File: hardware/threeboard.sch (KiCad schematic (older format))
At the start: 49 parts, among them J1 USB_mini_micro_B, K1 KEYSW, K2 KEYSW, K3 KEYSW, SW1 SW_PUSH, U1 ATMEGA32U4, U2 24LC512, X1 XTAL_GND

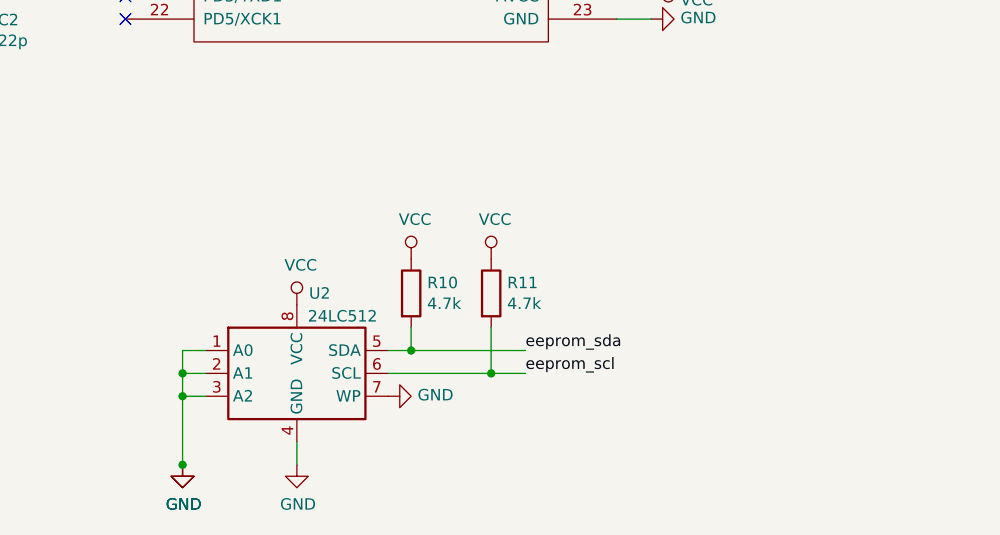
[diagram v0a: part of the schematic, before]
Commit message: Add v1 hardware revision with reinforced USB, better LED placement, and dual SMD EEPROM
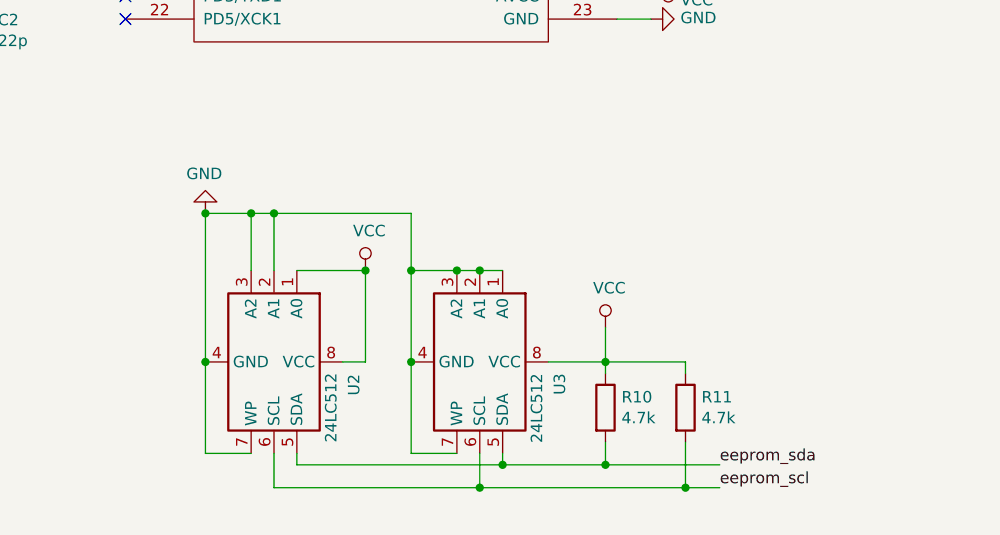
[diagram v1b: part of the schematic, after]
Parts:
- added U3: 24LC512, 24LC512-I_MF:DFN500X600X95-9N, symbol Memory_EEPROM:24LC512
- J1: footprint 10118194-0001LF:AMPHENOL_10118194-0001LF -> USB3070-XX-X_REVE:GCT_USB3070-XX-X_REVE
- SW1: footprint Button_Switch_SMD:SW_SPST_TL3342 -> PTS526_SK08_SMTR2_LFS:SW_PTS526_SK08_SMTR2_LFS
- U2: footprint 24LC512:SOIC127P794X203-8N -> 24LC512-I_MF:DFN500X600X95-9N
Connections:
- net GND: now also U3.1 (A0), U3.2 (A1), U3.3 (A2), U3.4 (GND), U3.7 (WP); no longer U2.1 (A0)
- net VCC: now also U2.1 (A0), U3.8 (VCC)
- net eeprom_scl: now also U3.6 (SCL)
- net eeprom_sda: now also U3.5 (SDA)
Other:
- moved on the sheet: R10, R11, U2
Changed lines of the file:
@@
 EESchema Schematic File Version 4
-LIBS:threeboard-cache
 EELAYER 30 0
 EELAYER END
@@
 F 0 "SW1" H 2000 4200 50  0000 C CNN
 F 1 "SW_PUSH" H 2000 4150 50  0001 C CNN
-F 2 "Button_Switch_SMD:SW_SPST_TL3342" H 2000 4250 60  0001 C CNN
+F 2 "PTS526_SK08_SMTR2_LFS:SW_PTS526_SK08_SMTR2_LFS" H 2000 4250 60  0001 C CNN
 F 3 "" H 2000 4250 60  0000 C CNN
 	1    2000 4250
@@
 F 0 "J1" H 1687 3591 60  0000 C CNN
 F 1 "USB_mini_micro_B" H 1650 3550 60  0001 C CNN
-F 2 "10118194-0001LF:AMPHENOL_10118194-0001LF" H 1750 3300 60  0001 C CNN
+F 2 "USB3070-XX-X_REVE:GCT_USB3070-XX-X_REVE" H 1750 3300 60  0001 C CNN
 F 3 "" H 1750 3300 60  0000 C CNN
 	1    1800 3300
@@
 NoConn ~ 4900 4250
 $Comp
-L power:GND #PWR0117
-U 1 1 5DEAE5F0
-P 3000 7100
-F 0 "#PWR0117" H 3000 6850 50  0001 C CNN
-F 1 "GND" H 3005 6927 50  0000 C CNN
-F 2 "" H 3000 7100 50  0001 C CNN
-F 3 "" H 3000 7100 50  0001 C CNN
-	1    3000 7100
-	1    0    0    -1
-$EndComp
-Wire Wire Line
-	3100 6600 3000 6600
-Wire Wire Line
-	3000 6600 3000 6700
-Wire Wire Line
-	3100 6700 3000 6700
-Connection ~ 3000 6700
-Wire Wire Line
-	3000 6700 3000 6800
-Wire Wire Line
-	3000 6800 3100 6800
-Connection ~ 3000 6800
-Wire Wire Line
-	3000 6800 3000 7100
-$Comp
-L power:GND #PWR0120
-U 1 1 5DEC54E2
-P 3000 7100
-F 0 "#PWR0120" H 3000 6850 50  0001 C CNN
-F 1 "GND" H 3005 6927 50  0000 C CNN
-F 2 "" H 3000 7100 50  0001 C CNN
-F 3 "" H 3000 7100 50  0001 C CNN
-	1    3000 7100
-	1    0    0    -1
-$EndComp
-Connection ~ 3000 7100
-$Comp
 L power:GND #PWR0121
 U 1 1 5DEC62E8
-P 3500 7100
-F 0 "#PWR0121" H 3500 6850 50  0001 C CNN
-F 1 "GND" H 3505 6927 50  0000 C CNN
-F 2 "" H 3500 7100 50  0001 C CNN
-F 3 "" H 3500 7100 50  0001 C CNN
-	1    3500 7100
-	1    0    0    -1
-$EndComp
-Wire Wire Line
-	3500 7000 3500 7100
-$Comp
-L power:GND #PWR0122
-U 1 1 5DED20A3
-P 3900 6800
-F 0 "#PWR0122" H 3900 6550 50  0001 C CNN
-F 1 "GND" V 3905 6672 50  0000 R CNN
-F 2 "" H 3900 6800 50  0001 C CNN
-F 3 "" H 3900 6800 50  0001 C CNN
-	1    3900 6800
-	0    -1   -1   0
-$EndComp
-$Comp
-L power:VCC #PWR0123
-U 1 1 5DED2ECF
-P 3500 6400
-F 0 "#PWR0123" H 3500 6250 50  0001 C CNN
-F 1 "VCC" H 3517 6573 50  0000 C CNN
-F 2 "" H 3500 6400 50  0001 C CNN
-F 3 "" H 3500 6400 50  0001 C CNN
-	1    3500 6400
-	1    0    0    -1
-$EndComp
-$Comp
-L Memory_EEPROM:24LC512 U2
-U 1 1 5DEACBF7
-P 3500 6700
-F 0 "U2" H 3600 7050 50  0000 C CNN
-F 1 "24LC512" H 3700 6950 50  0000 C CNN
-F 2 "24LC512:SOIC127P794X203-8N" H 3500 6700 50  0001 C CNN
-F 3 "http://ww1.microchip.com/downloads/en/DeviceDoc/21754M.pdf" H 3500 6700 50  0001 C CNN
-	1    3500 6700
-	1    0    0    -1
-$EndComp
-Text Label 4500 6700 0    50   ~ 0
+P 3100 6000
+F 0 "#PWR0121" H 3100 5750 50  0001 C CNN
+F 1 "GND" H 3105 5827 50  0000 C CNN
+F 2 "" H 3100 6000 50  0001 C CNN
+F 3 "" H 3100 6000 50  0001 C CNN
+	1    3100 6000
+	-1   0    0    1
+$EndComp
+Text Label 5350 7200 0    50   ~ 0
 eeprom_scl
 $Comp
 L Device:R R10
 U 1 1 5DEE15C4
-P 4000 6350
-F 0 "R10" H 4070 6396 50  0000 L CNN
-F 1 "4.7k" H 4070 6305 50  0000 L CNN
-F 2 "Resistor_SMD:R_0805_2012Metric_Pad1.15x1.40mm_HandSolder" V 3930 6350 50  0001 C CNN
-F 3 "~" H 4000 6350 50  0001 C CNN
-	1    4000 6350
-	1    0    0    -1
-$EndComp
-$Comp
-L power:VCC #PWR0124
-U 1 1 5DEE1CFE
-P 4000 6200
-F 0 "#PWR0124" H 4000 6050 50  0001 C CNN
-F 1 "VCC" H 4017 6373 50  0000 C CNN
-F 2 "" H 4000 6200 50  0001 C CNN
-F 3 "" H 4000 6200 50  0001 C CNN
-	1    4000 6200
-	1    0    0    -1
-$EndComp
-Wire Wire Line
-	3900 6600 4000 6600
-Wire Wire Line
-	4000 6600 4000 6500
-Text Label 4500 6600 0    50   ~ 0
+P 4850 6850
+F 0 "R10" H 4920 6896 50  0000 L CNN
+F 1 "4.7k" H 4920 6805 50  0000 L CNN
+F 2 "Resistor_SMD:R_0805_2012Metric_Pad1.15x1.40mm_HandSolder" V 4780 6850 50  0001 C CNN
+F 3 "~" H 4850 6850 50  0001 C CNN
+	1    4850 6850
+	1    0    0    -1
+$EndComp
+Wire Wire Line
+	4850 7100 4850 7000
+Text Label 5350 7100 0    50   ~ 0
 eeprom_sda
-Connection ~ 4000 6600
+Connection ~ 4850 7100
 $Comp
 L Device:C_Small C4
@@
 L Device:R R11
 U 1 1 5E419777
-P 4350 6350
-F 0 "R11" H 4420 6396 50  0000 L CNN
-F 1 "4.7k" H 4420 6305 50  0000 L CNN
-F 2 "Resistor_SMD:R_0805_2012Metric_Pad1.15x1.40mm_HandSolder" V 4280 6350 50  0001 C CNN
-F 3 "~" H 4350 6350 50  0001 C CNN
-	1    4350 6350
-	1    0    0    -1
-$EndComp
-Wire Wire Line
-	4000 6600 4500 6600
-Wire Wire Line
-	3900 6700 4350 6700
-Wire Wire Line
-	4350 6500 4350 6700
-Connection ~ 4350 6700
-Wire Wire Line
-	4350 6700 4500 6700
-$Comp
-L power:VCC #PWR0125
-U 1 1 5E430356
-P 4350 6200
-F 0 "#PWR0125" H 4350 6050 50  0001 C CNN
-F 1 "VCC" H 4367 6373 50  0000 C CNN
-F 2 "" H 4350 6200 50  0001 C CNN
-F 3 "" H 4350 6200 50  0001 C CNN
-	1    4350 6200
-	1    0    0    -1
-$EndComp
+P 5200 6850
+F 0 "R11" H 5270 6896 50  0000 L CNN
+F 1 "4.7k" H 5270 6805 50  0000 L CNN
+F 2 "Resistor_SMD:R_0805_2012Metric_Pad1.15x1.40mm_HandSolder" V 5130 6850 50  0001 C CNN
+F 3 "~" H 5200 6850 50  0001 C CNN
+	1    5200 6850
+	1    0    0    -1
+$EndComp
+Wire Wire Line
+	4850 7100 5350 7100
+Wire Wire Line
+	5200 7000 5200 7200
+Connection ~ 5200 7200
+Wire Wire Line
+	5200 7200 5350 7200
 Text Label 4900 4550 0    50   ~ 0
 row4
@@
 Text Label 4900 3650 0    50   ~ 0
 col3
+$Comp
+L Memory_EEPROM:24LC512 U3
+U 1 1 5E8FC903
+P 4300 6650
+F 0 "U3" H 4350 7000 50  0000 L CNN
+F 1 "24LC512" H 4350 6900 50  0000 L CNN
+F 2 "24LC512-I_MF:DFN500X600X95-9N" H 4300 6650 50  0001 C CNN
+F 3 "http://ww1.microchip.com/downloads/en/DeviceDoc/21754M.pdf" H 4300 6650 50  0001 C CNN
+	1    4300 6650
+	0    1    1    0
+$EndComp
+Wire Wire Line
+	4400 6250 4300 6250
+Wire Wire Line
+	4300 6250 4200 6250
+Connection ~ 4300 6250
+Wire Wire Line
+	4200 6250 4000 6250
+Connection ~ 4200 6250
+Wire Wire Line
+	4000 6650 4000 6250
+Wire Wire Line
+	4200 7050 4000 7050
+Wire Wire Line
+	4000 7050 4000 6650
+Connection ~ 4000 6650
+Wire Wire Line
+	3300 7050 3100 7050
+Wire Wire Line
+	3400 7200 4300 7200
+Wire Wire Line
+	4300 7050 4300 7200
+Connection ~ 4300 7200
+Wire Wire Line
+	4300 7200 5200 7200
+Wire Wire Line
+	3500 7050 3500 7100
+Wire Wire Line
+	3500 7100 4400 7100
+Wire Wire Line
+	4400 7050 4400 7100
+Connection ~ 4400 7100
+Wire Wire Line
+	4400 7100 4850 7100
+Wire Wire Line
+	4600 6650 4850 6650
+Wire Wire Line
+	4850 6650 4850 6700
+Connection ~ 4850 6650
+Wire Wire Line
+	4850 6650 5200 6650
+Wire Wire Line
+	5200 6650 5200 6700
+$Comp
+L power:VCC #PWR0117
+U 1 1 5E9F15CD
+P 3800 6250
+F 0 "#PWR0117" H 3800 6100 50  0001 C CNN
+F 1 "VCC" H 3817 6423 50  0000 C CNN
+F 2 "" H 3800 6250 50  0001 C CNN
+F 3 "" H 3800 6250 50  0001 C CNN
+	1    3800 6250
+	1    0    0    -1
+$EndComp
+Wire Wire Line
+	3800 6650 3700 6650
+$Comp
+L power:VCC #PWR0124
+U 1 1 5DEE1CFE
+P 4850 6500
+F 0 "#PWR0124" H 4850 6350 50  0001 C CNN
+F 1 "VCC" H 4867 6673 50  0000 C CNN
+F 2 "" H 4850 6500 50  0001 C CNN
+F 3 "" H 4850 6500 50  0001 C CNN
+	1    4850 6500
+	1    0    0    -1
+$EndComp
+Wire Wire Line
+	4850 6500 4850 6650
+Wire Wire Line
+	3100 6650 3100 7050
+Wire Wire Line
+	3400 7050 3400 7200
+$Comp
+L Memory_EEPROM:24LC512 U2
+U 1 1 5DEACBF7
+P 3400 6650
+F 0 "U2" H 3500 7000 50  0000 C CNN
+F 1 "24LC512" H 3600 6900 50  0000 C CNN
+F 2 "24LC512-I_MF:DFN500X600X95-9N" H 3400 6650 50  0001 C CNN
+F 3 "http://ww1.microchip.com/downloads/en/DeviceDoc/21754M.pdf" H 3400 6650 50  0001 C CNN
+	1    3400 6650
+	0    1    1    0
+$EndComp
+Wire Wire Line
+	3500 6250 3800 6250
+Wire Wire Line
+	3800 6250 3800 6650
+Connection ~ 3800 6250
+Wire Wire Line
+	3400 6250 3400 6000
+Wire Wire Line
+	3400 6000 3300 6000
+Connection ~ 3400 6000
+Wire Wire Line
+	3300 6250 3300 6000
+Connection ~ 3300 6000
+Wire Wire Line
+	3300 6000 3100 6000
+Wire Wire Line
+	3400 6000 4000 6000
+Wire Wire Line
+	4000 6000 4000 6250
+Connection ~ 4000 6250
+Wire Wire Line
+	3100 6650 3100 6000
+Connection ~ 3100 6650
+Connection ~ 3100 6000
 $EndSCHEMATC
